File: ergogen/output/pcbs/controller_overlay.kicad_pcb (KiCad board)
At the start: 2 copper layers, 19.7 x 60.5 mm, 2 parts

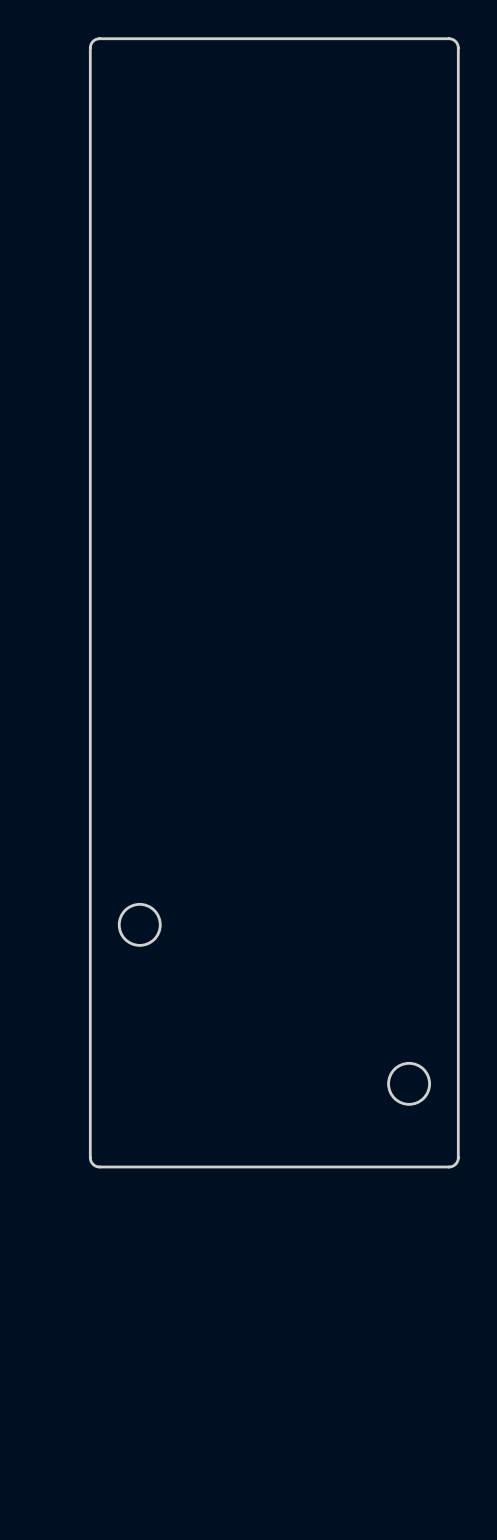
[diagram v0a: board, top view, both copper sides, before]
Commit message: feat: souffle outputs
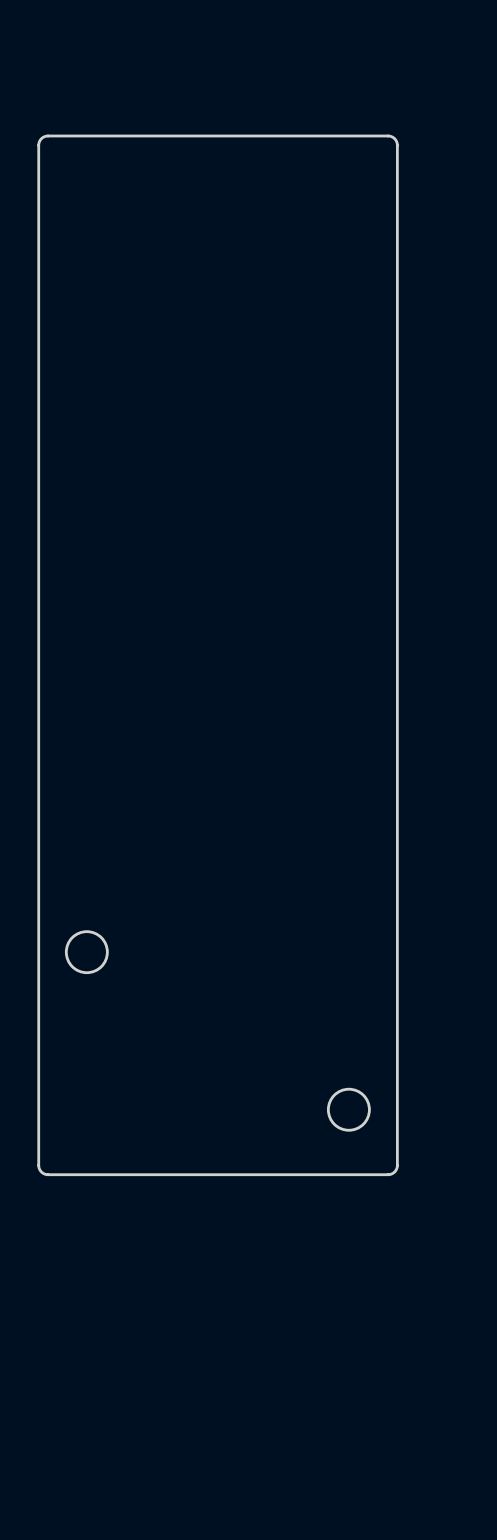
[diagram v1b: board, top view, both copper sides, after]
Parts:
- moved MH2 3.51 mm to (219.0, 91.4)
- moved MH1 3.19 mm to (204.9, 82.9)
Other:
- board size 19.7 x 60.5 mm -> 19.2 x 55.7 mm
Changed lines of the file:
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@@
   (title_block
     (title "controller_overlay")
-    (date "2025-02-05")
+    (date "2025-02-06")
     (rev "0.1")
-    (company "ceoloide (adapted from corney-island)")
+    (company "fcoury (adapted from corney-island)")
   )
   (layers
@@
   (footprint "ceoloide:mounting_hole_npth"
     (layer "F.Cu")
-    (at 207.762 81.476 0)
+    (at 204.927 82.9385 0)
     (property "Reference" "MH1"
       (at 0 2.55 0)
@@
   (footprint "ceoloide:mounting_hole_npth"
     (layer "F.Cu")
-    (at 222.194 89.995 0)
+    (at 218.969 91.3825 0)
     (property "Reference" "MH2"
       (at 0 2.55 0)
@@
     )
   )
-  (gr_line (start 205.113 93.951) (end 205.113 34.49) (layer Edge.Cuts) (stroke (width 0.15) (type default)))
-(gr_line (start 205.613 33.99) (end 224.333 33.99) (layer Edge.Cuts) (stroke (width 0.15) (type default)))
-(gr_line (start 224.833 34.49) (end 224.833 93.951) (layer Edge.Cuts) (stroke (width 0.15) (type default)))
-(gr_line (start 224.333 94.451) (end 205.613 94.451) (layer Edge.Cuts) (stroke (width 0.15) (type default)))
-(gr_arc (start 205.613 33.99) (mid 205.2594466 34.1364466) (end 205.113 34.49) (layer Edge.Cuts) (stroke (width 0.15) (type default)))
-(gr_arc (start 224.833 34.49) (mid 224.6865534 34.1364466) (end 224.333 33.99) (layer Edge.Cuts) (stroke (width 0.15) (type default)))
-(gr_arc (start 224.333 94.451) (mid 224.6865534 94.30455339999999) (end 224.833 93.951) (layer Edge.Cuts) (stroke (width 0.15) (type default)))
-(gr_arc (start 205.113 93.951) (mid 205.2594466 94.30455339999999) (end 205.613 94.451) (layer Edge.Cuts) (stroke (width 0.15) (type default)))
-(gr_circle (center 207.762 81.476) (end 208.862 81.476) (layer Edge.Cuts) (stroke (width 0.15) (type default)) (fill none))
-(gr_circle (center 222.194 89.995) (end 223.29399999999998 89.995) (layer Edge.Cuts) (stroke (width 0.15) (type default)) (fill none))
+  (gr_line (start 202.348 94.3635) (end 202.348 39.7025) (layer Edge.Cuts) (stroke (width 0.15) (type default)))
+(gr_line (start 202.848 39.2025) (end 221.068 39.2025) (layer Edge.Cuts) (stroke (width 0.15) (type default)))
+(gr_line (start 221.568 39.7025) (end 221.568 94.3635) (layer Edge.Cuts) (stroke (width 0.15) (type default)))
+(gr_line (start 221.068 94.8635) (end 202.848 94.8635) (layer Edge.Cuts) (stroke (width 0.15) (type default)))
+(gr_arc (start 202.848 39.2025) (mid 202.4944466 39.3489466) (end 202.348 39.7025) (layer Edge.Cuts) (stroke (width 0.15) (type default)))
+(gr_arc (start 221.568 39.7025) (mid 221.42155340000002 39.3489466) (end 221.068 39.2025) (layer Edge.Cuts) (stroke (width 0.15) (type default)))
+(gr_arc (start 221.068 94.8635) (mid 221.42155340000002 94.7170534) (end 221.568 94.3635) (layer Edge.Cuts) (stroke (width 0.15) (type default)))
+(gr_arc (start 202.348 94.3635) (mid 202.4944466 94.7170534) (end 202.848 94.8635) (layer Edge.Cuts) (stroke (width 0.15) (type default)))
+(gr_circle (center 204.927 82.9385) (end 206.027 82.9385) (layer Edge.Cuts) (stroke (width 0.15) (type default)) (fill none))
+(gr_circle (center 218.969 91.3825) (end 220.069 91.3825) (layer Edge.Cuts) (stroke (width 0.15) (type default)) (fill none))
 )

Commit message: fix: number row on top and improved outline
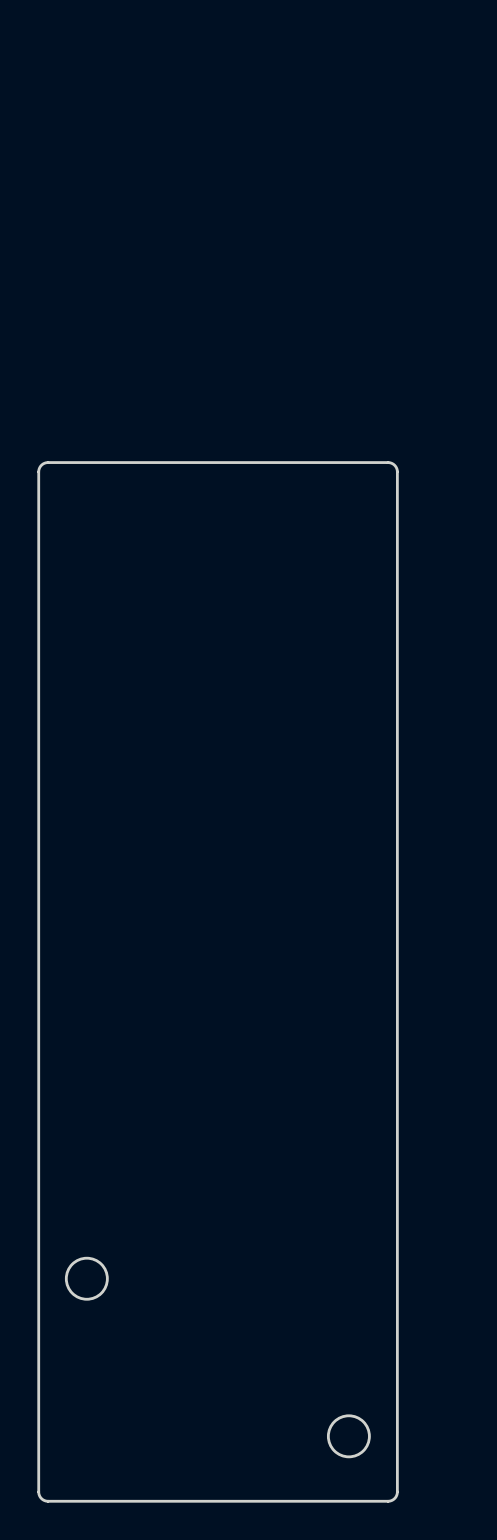
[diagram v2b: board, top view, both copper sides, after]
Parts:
- moved MH1 17.5 mm to (204.9, 100.4)
- moved MH2 17.5 mm to (219.0, 108.9)
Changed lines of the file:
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@@
   (footprint "ceoloide:mounting_hole_npth"
     (layer "F.Cu")
-    (at 204.927 82.9385 0)
+    (at 204.927 100.4385 0)
     (property "Reference" "MH1"
       (at 0 2.55 0)
@@
   (footprint "ceoloide:mounting_hole_npth"
     (layer "F.Cu")
-    (at 218.969 91.3825 0)
+    (at 218.969 108.8825 0)
     (property "Reference" "MH2"
       (at 0 2.55 0)
@@
     )
   )
-  (gr_line (start 202.348 94.3635) (end 202.348 39.7025) (layer Edge.Cuts) (stroke (width 0.15) (type default)))
-(gr_line (start 202.848 39.2025) (end 221.068 39.2025) (layer Edge.Cuts) (stroke (width 0.15) (type default)))
-(gr_line (start 221.568 39.7025) (end 221.568 94.3635) (layer Edge.Cuts) (stroke (width 0.15) (type default)))
-(gr_line (start 221.068 94.8635) (end 202.848 94.8635) (layer Edge.Cuts) (stroke (width 0.15) (type default)))
-(gr_arc (start 202.848 39.2025) (mid 202.4944466 39.3489466) (end 202.348 39.7025) (layer Edge.Cuts) (stroke (width 0.15) (type default)))
-(gr_arc (start 221.568 39.7025) (mid 221.42155340000002 39.3489466) (end 221.068 39.2025) (layer Edge.Cuts) (stroke (width 0.15) (type default)))
-(gr_arc (start 221.068 94.8635) (mid 221.42155340000002 94.7170534) (end 221.568 94.3635) (layer Edge.Cuts) (stroke (width 0.15) (type default)))
-(gr_arc (start 202.348 94.3635) (mid 202.4944466 94.7170534) (end 202.848 94.8635) (layer Edge.Cuts) (stroke (width 0.15) (type default)))
-(gr_circle (center 204.927 82.9385) (end 206.027 82.9385) (layer Edge.Cuts) (stroke (width 0.15) (type default)) (fill none))
-(gr_circle (center 218.969 91.3825) (end 220.069 91.3825) (layer Edge.Cuts) (stroke (width 0.15) (type default)) (fill none))
+  (gr_line (start 202.348 111.8635) (end 202.348 57.2025) (layer Edge.Cuts) (stroke (width 0.15) (type default)))
+(gr_line (start 202.848 56.7025) (end 221.068 56.7025) (layer Edge.Cuts) (stroke (width 0.15) (type default)))
+(gr_line (start 221.568 57.2025) (end 221.568 111.8635) (layer Edge.Cuts) (stroke (width 0.15) (type default)))
+(gr_line (start 221.068 112.3635) (end 202.848 112.3635) (layer Edge.Cuts) (stroke (width 0.15) (type default)))
+(gr_arc (start 202.848 56.7025) (mid 202.4944466 56.8489466) (end 202.348 57.2025) (layer Edge.Cuts) (stroke (width 0.15) (type default)))
+(gr_arc (start 221.568 57.2025) (mid 221.42155340000002 56.8489466) (end 221.068 56.7025) (layer Edge.Cuts) (stroke (width 0.15) (type default)))
+(gr_arc (start 221.068 112.3635) (mid 221.42155340000002 112.2170534) (end 221.568 111.8635) (layer Edge.Cuts) (stroke (width 0.15) (type default)))
+(gr_arc (start 202.348 111.8635) (mid 202.4944466 112.2170534) (end 202.848 112.3635) (layer Edge.Cuts) (stroke (width 0.15) (type default)))
+(gr_circle (center 204.927 100.4385) (end 206.027 100.4385) (layer Edge.Cuts) (stroke (width 0.15) (type default)) (fill none))
+(gr_circle (center 218.969 108.8825) (end 220.069 108.8825) (layer Edge.Cuts) (stroke (width 0.15) (type default)) (fill none))
 )

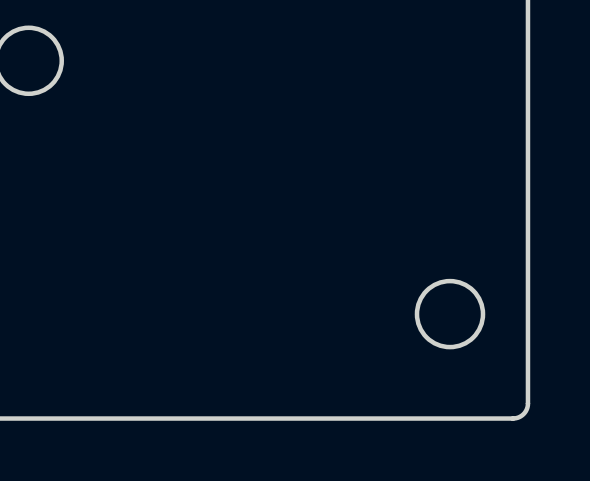
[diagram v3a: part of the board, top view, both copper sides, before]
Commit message: feat: adjusted the screw hole instead
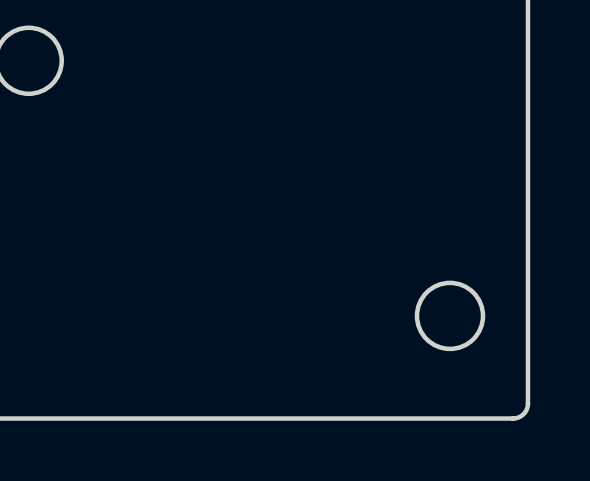
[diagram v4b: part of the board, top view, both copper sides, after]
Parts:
- moved MH2 0.06 mm to (219.0, 108.9)
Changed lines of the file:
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@@
   (footprint "ceoloide:mounting_hole_npth"
     (layer "F.Cu")
-    (at 218.969 108.8825 0)
+    (at 218.969 108.9425 0)
     (property "Reference" "MH2"
       (at 0 2.55 0)
@@
 (gr_arc (start 202.348 111.8635) (mid 202.4944466 112.2170534) (end 202.848 112.3635) (layer Edge.Cuts) (stroke (width 0.15) (type default)))
 (gr_circle (center 204.927 100.4385) (end 206.027 100.4385) (layer Edge.Cuts) (stroke (width 0.15) (type default)) (fill none))
-(gr_circle (center 218.969 108.8825) (end 220.069 108.8825) (layer Edge.Cuts) (stroke (width 0.15) (type default)) (fill none))
+(gr_circle (center 218.969 108.9425) (end 220.069 108.9425) (layer Edge.Cuts) (stroke (width 0.15) (type default)) (fill none))
 )

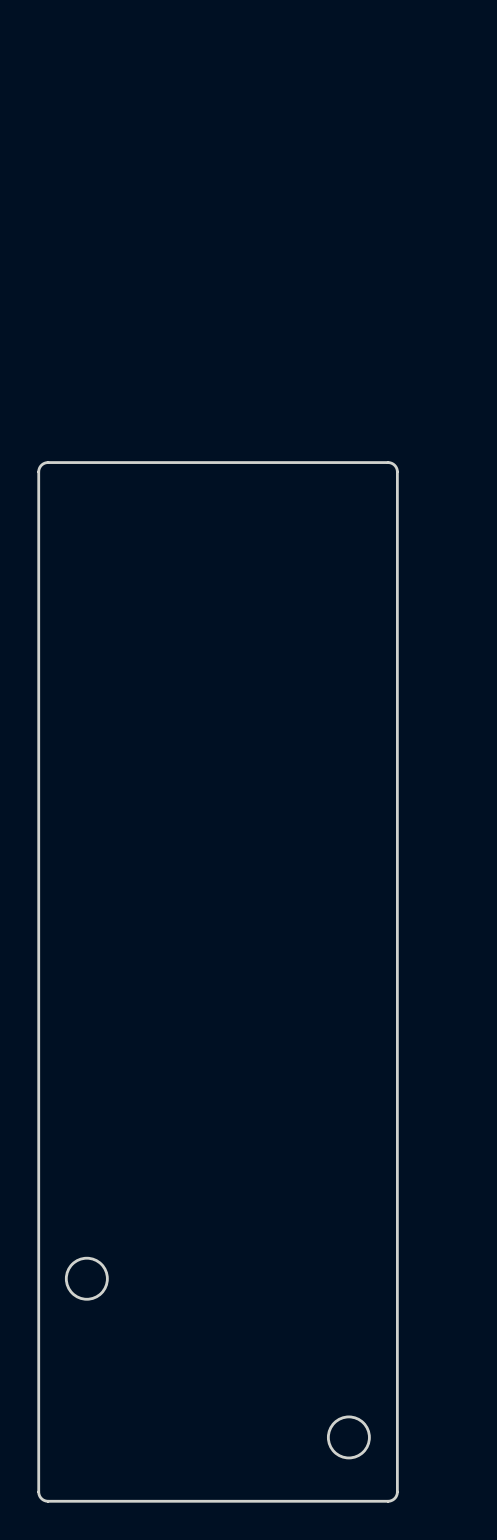
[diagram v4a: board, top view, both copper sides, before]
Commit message: feat: PCB holes alignment
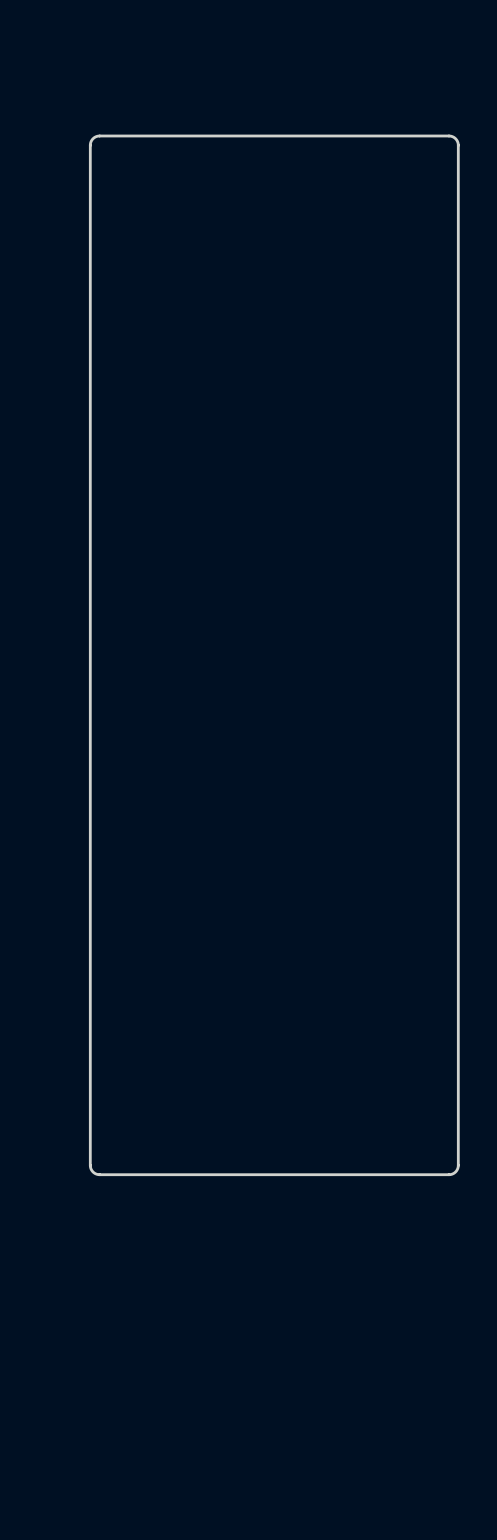
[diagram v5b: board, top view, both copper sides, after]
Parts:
- removed MH1, MH2: , ceoloide:mounting_hole_npth
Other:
- board size 19.2 x 55.7 mm -> 19.7 x 55.7 mm
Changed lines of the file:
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@@
   (title_block
     (title "controller_overlay")
-    (date "2025-02-07")
+    (date "2025-02-11")
     (rev "0.1")
     (company "fcoury (adapted from corney-island)")
@@
   )
   (net 0 "")
-  (footprint "ceoloide:mounting_hole_npth"
-    (layer "F.Cu")
-    (at 204.927 100.4385 0)
-    (property "Reference" "MH1"
-      (at 0 2.55 0)
-      (layer "F.SilkS")
-      hide
-      (effects (font (size 1 1) (thickness 0.15)))
-    )
-    (pad "" np_thru_hole circle
-      (at 0 0 0)
-      (size 2.2 2.2)
-      (drill 2.2)
-      (layers "*.Cu" "*.Mask")
-    )
-  )
-  (footprint "ceoloide:mounting_hole_npth"
-    (layer "F.Cu")
-    (at 218.969 108.9425 0)
-    (property "Reference" "MH2"
-      (at 0 2.55 0)
-      (layer "F.SilkS")
-      hide
-      (effects (font (size 1 1) (thickness 0.15)))
-    )
-    (pad "" np_thru_hole circle
-      (at 0 0 0)
-      (size 2.2 2.2)
-      (drill 2.2)
-      (layers "*.Cu" "*.Mask")
-    )
-  )
-  (gr_line (start 202.348 111.8635) (end 202.348 57.2025) (layer Edge.Cuts) (stroke (width 0.15) (type default)))
-(gr_line (start 202.848 56.7025) (end 221.068 56.7025) (layer Edge.Cuts) (stroke (width 0.15) (type default)))
-(gr_line (start 221.568 57.2025) (end 221.568 111.8635) (layer Edge.Cuts) (stroke (width 0.15) (type default)))
-(gr_line (start 221.068 112.3635) (end 202.848 112.3635) (layer Edge.Cuts) (stroke (width 0.15) (type default)))
-(gr_arc (start 202.848 56.7025) (mid 202.4944466 56.8489466) (end 202.348 57.2025) (layer Edge.Cuts) (stroke (width 0.15) (type default)))
-(gr_arc (start 221.568 57.2025) (mid 221.42155340000002 56.8489466) (end 221.068 56.7025) (layer Edge.Cuts) (stroke (width 0.15) (type default)))
-(gr_arc (start 221.068 112.3635) (mid 221.42155340000002 112.2170534) (end 221.568 111.8635) (layer Edge.Cuts) (stroke (width 0.15) (type default)))
-(gr_arc (start 202.348 111.8635) (mid 202.4944466 112.2170534) (end 202.848 112.3635) (layer Edge.Cuts) (stroke (width 0.15) (type default)))
-(gr_circle (center 204.927 100.4385) (end 206.027 100.4385) (layer Edge.Cuts) (stroke (width 0.15) (type default)) (fill none))
-(gr_circle (center 218.969 108.9425) (end 220.069 108.9425) (layer Edge.Cuts) (stroke (width 0.15) (type default)) (fill none))
+  (gr_line (start 205.113 94.3635) (end 205.113 39.7025) (layer Edge.Cuts) (stroke (width 0.15) (type default)))
+(gr_line (start 205.613 39.2025) (end 224.333 39.2025) (layer Edge.Cuts) (stroke (width 0.15) (type default)))
+(gr_line (start 224.833 39.7025) (end 224.833 94.3635) (layer Edge.Cuts) (stroke (width 0.15) (type default)))
+(gr_line (start 224.333 94.8635) (end 205.613 94.8635) (layer Edge.Cuts) (stroke (width 0.15) (type default)))
+(gr_arc (start 205.613 39.2025) (mid 205.2594466 39.3489466) (end 205.113 39.7025) (layer Edge.Cuts) (stroke (width 0.15) (type default)))
+(gr_arc (start 224.833 39.7025) (mid 224.6865534 39.3489466) (end 224.333 39.2025) (layer Edge.Cuts) (stroke (width 0.15) (type default)))
+(gr_arc (start 224.333 94.8635) (mid 224.6865534 94.7170534) (end 224.833 94.3635) (layer Edge.Cuts) (stroke (width 0.15) (type default)))
+(gr_arc (start 205.113 94.3635) (mid 205.2594466 94.7170534) (end 205.613 94.8635) (layer Edge.Cuts) (stroke (width 0.15) (type default)))
 )
